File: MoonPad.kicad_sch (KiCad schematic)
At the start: 56 parts, among them IC1 W25Q16JVUXIQ, J1 OLED, J3 USB-C 2.0 Receptacle, SW1 Reset, U3 RP2040, U4 Hall_Sensor, U5 Hall_Sensor, U6 AP2112K-3.3, Y1 JGHC S3212000181080

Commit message: Added fuse
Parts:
- added D7: PRTR5V0U2X, Package_TO_SOT_SMD:SOT-143, symbol Power_Protection:PRTR5V0U2X
- added F1: Polyfuse, Fuse:Fuse_1206_3216Metric, symbol Device:Polyfuse
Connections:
- net GND: now also D7.1 (GND)
- net USB_D+: now also D7.2 (I/O1)
- net USB_D-: now also D7.3 (I/O2)
- net VBUS: now also D7.4 (VCC), F1.2; no longer J3.A4 (VBUS), J3.A9 (VBUS), J3.B4 (VBUS), J3.B9 (VBUS)
- new net Fuse: F1.1, J3.A4 (VBUS), J3.A9 (VBUS), J3.B4 (VBUS), J3.B9 (VBUS)
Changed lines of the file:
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@@
   (junction (at 207.01 81.28) (diameter 0) (color 0 0 0 0)
   )
-  (junction (at 57.15 35.56) (diameter 0) (color 0 0 0 0)
+  (junction (at 62.23 35.56) (diameter 0) (color 0 0 0 0)
   )
   (junction (at 355.6 160.02) (diameter 0) (color 0 0 0 0)
@@
     (stroke (width 0) (type default))
   )
-  (wire (pts (xy 57.15 34.29) (xy 57.15 35.56))
+  (wire (pts (xy 62.23 34.29) (xy 62.23 35.56))
     (stroke (width 0) (type default))
   )
@@
     (stroke (width 0) (type default))
   )
+  (wire (pts (xy 83.82 50.8) (xy 83.82 71.12))
+    (stroke (width 0) (type default))
+  )
   (wire (pts (xy 168.91 60.96) (xy 177.8 60.96))
     (stroke (width 0) (type default))
@@
     (stroke (width 0) (type default))
   )
+  (wire (pts (xy 59.69 35.56) (xy 62.23 35.56))
+    (stroke (width 0) (type default))
+  )
   (wire (pts (xy 204.47 81.28) (xy 207.01 81.28))
     (stroke (width 0) (type default))
@@
     (stroke (width 0) (type default))
   )
-  (wire (pts (xy 57.15 35.56) (xy 67.31 35.56))
+  (wire (pts (xy 62.23 35.56) (xy 67.31 35.56))
     (stroke (width 0) (type default))
   )
@@
     (stroke (width 0) (type default))
   )
+  (wire (pts (xy 52.07 35.56) (xy 49.53 35.56))
+    (stroke (width 0) (type default))
+  )
   (wire (pts (xy 67.31 44.45) (xy 67.31 45.72))
     (stroke (width 0) (type default))
   )
-  (wire (pts (xy 49.53 50.8) (xy 58.42 50.8))
+  (wire (pts (xy 49.53 50.8) (xy 83.82 50.8))
     (stroke (width 0) (type default))
   )
@@
     (stroke (width 0) (type default))
   )
+  (wire (pts (xy 58.42 55.88) (xy 58.42 71.12))
+    (stroke (width 0) (type default))
+  )
   (wire (pts (xy 269.24 62.23) (xy 269.24 60.96))
     (stroke (width 0) (type default))
@@
     (stroke (width 0) (type default))
   )
-  (wire (pts (xy 49.53 35.56) (xy 57.15 35.56))
-    (stroke (width 0) (type default))
-  )
   (wire (pts (xy 229.87 101.6) (xy 236.22 101.6))
     (stroke (width 0) (type default))
@@
     (effects (font (size 1.27 1.27)) (justify right bottom))
   )
+  (label "Fuse" (at 49.53 35.56 0) (fields_autoplaced)
+    (effects (font (size 1.27 1.27)) (justify left bottom))
+  )
   (label "USB_D+" (at 262.89 96.52 180) (fields_autoplaced)
     (effects (font (size 1.27 1.27)) (justify right bottom))
@@
     )
   )
-  (symbol (lib_id "power:VBUS") (at 57.15 34.29 0) (unit 1)
+  (symbol (lib_id "power:VBUS") (at 62.23 34.29 0) (unit 1)
     (in_bom yes) (on_board yes) (dnp no)
-    (property "Reference" "#PWR03" (at 57.15 38.1 0)
+    (property "Reference" "#PWR03" (at 62.23 38.1 0)
       (effects (font (size 1.27 1.27)) hide)
     )
-    (property "Value" "VBUS" (at 57.15 30.48 0)
+    (property "Value" "VBUS" (at 62.23 30.48 0)
       (effects (font (size 1.27 1.27)))
     )
-    (property "Footprint" "" (at 57.15 34.29 0)
+    (property "Footprint" "" (at 62.23 34.29 0)
       (effects (font (size 1.27 1.27)) hide)
     )
-    (property "Datasheet" "" (at 57.15 34.29 0)
+    (property "Datasheet" "" (at 62.23 34.29 0)
       (effects (font (size 1.27 1.27)) hide)
     )
@@
     )
   )
+  (symbol (lib_id "power:GND") (at 71.12 83.82 0) (unit 1)
+    (in_bom yes) (on_board yes) (dnp no) (fields_autoplaced)
+    (property "Reference" "#PWR047" (at 71.12 90.17 0)
+      (effects (font (size 1.27 1.27)) hide)
+    )
+    (property "Value" "GND" (at 71.12 88.9 0)
+      (effects (font (size 1.27 1.27)))
+    )
+    (property "Footprint" "" (at 71.12 83.82 0)
+      (effects (font (size 1.27 1.27)) hide)
+    )
+    (property "Datasheet" "" (at 71.12 83.82 0)
+      (effects (font (size 1.27 1.27)) hide)
+    )
+    (pin "1")
+    (instances
+      (project "MoonPad"
+        (path "/66a337f3-0e1a-4778-bb9f-853ccc5d3181"
+          (reference "#PWR047") (unit 1)
+        )
+      )
+    )
+  )
   (symbol (lib_id "power:GND") (at 69.85 124.46 0) (unit 1)
     (in_bom yes) (on_board yes) (dnp no)
@@
     )
   )
+  (symbol (lib_id "Device:Polyfuse") (at 55.88 35.56 90) (unit 1)
+    (in_bom yes) (on_board yes) (dnp no) (fields_autoplaced)
+    (property "Reference" "F1" (at 55.88 30.48 90)
+      (effects (font (size 1.27 1.27)))
+    )
+    (property "Value" "Polyfuse" (at 55.88 33.02 90)
+      (effects (font (size 1.27 1.27)))
+    )
+    (property "Footprint" "Fuse:Fuse_1206_3216Metric" (at 60.96 34.29 0)
+      (effects (font (size 1.27 1.27)) (justify left) hide)
+    )
+    (property "Datasheet" "https://datasheet.lcsc.com/lcsc/2103221807_BNstar-SMD1206-110C-24V_C2760273.pdf" (at 55.88 35.56 0)
+      (effects (font (size 1.27 1.27)) hide)
+    )
+    (property "LCSC Part" "https://www.lcsc.com/product-detail/Resettable-Fuses_BNstar-SMD1206-110C-24V_C2760273.html" (at 55.88 35.56 90)
+      (effects (font (size 1.27 1.27)) hide)
+    )
+    (pin "1")
+    (pin "2")
+    (instances
+      (project "MoonPad"
+        (path "/66a337f3-0e1a-4778-bb9f-853ccc5d3181"
+          (reference "F1") (unit 1)
+        )
+      )
+    )
+  )
   (symbol (lib_id "power:GND") (at 170.18 234.95 0) (unit 1)
     (in_bom yes) (on_board yes) (dnp no) (fields_autoplaced)
@@
     )
   )
+  (symbol (lib_id "Power_Protection:PRTR5V0U2X") (at 71.12 71.12 0) (unit 1)
+    (in_bom yes) (on_board yes) (dnp no) (fields_autoplaced)
+    (property "Reference" "D7" (at 86.36 69.1897 0)
+      (effects (font (size 1.27 1.27)))
+    )
+    (property "Value" "PRTR5V0U2X" (at 86.36 71.7297 0)
+      (effects (font (size 1.27 1.27)))
+    )
+    (property "Footprint" "Package_TO_SOT_SMD:SOT-143" (at 72.644 71.12 0)
+      (effects (font (size 1.27 1.27)) hide)
+    )
+    (property "Datasheet" "https://assets.nexperia.com/documents/data-sheet/PRTR5V0U2X.pdf" (at 72.644 71.12 0)
+      (effects (font (size 1.27 1.27)) hide)
+    )
+    (pin "1")
+    (pin "2")
+    (pin "3")
+    (pin "4")
+    (instances
+      (project "MoonPad"
+        (path "/66a337f3-0e1a-4778-bb9f-853ccc5d3181"
+          (reference "D7") (unit 1)
+        )
+      )
+    )
+  )
   (symbol (lib_id "Device:R") (at 59.69 116.84 270) (unit 1)
     (in_bom yes) (on_board yes) (dnp no)
@@
         )
       )
+    )
+  )
+  (symbol (lib_id "power:VBUS") (at 71.12 58.42 0) (unit 1)
+    (in_bom yes) (on_board yes) (dnp no)
+    (property "Reference" "#PWR048" (at 71.12 62.23 0)
+      (effects (font (size 1.27 1.27)) hide)
+    )
+    (property "Value" "VBUS" (at 71.12 54.61 0)
+      (effects (font (size 1.27 1.27)))
+    )
+    (property "Footprint" "" (at 71.12 58.42 0)
+      (effects (font (size 1.27 1.27)) hide)
+    )
+    (property "Datasheet" "" (at 71.12 58.42 0)
+      (effects (font (size 1.27 1.27)) hide)
+    )
+    (pin "1")
+    (instances
+      (project "MoonPad"
+        (path "/66a337f3-0e1a-4778-bb9f-853ccc5d3181"
+          (reference "#PWR048") (unit 1)
+        )
+      )

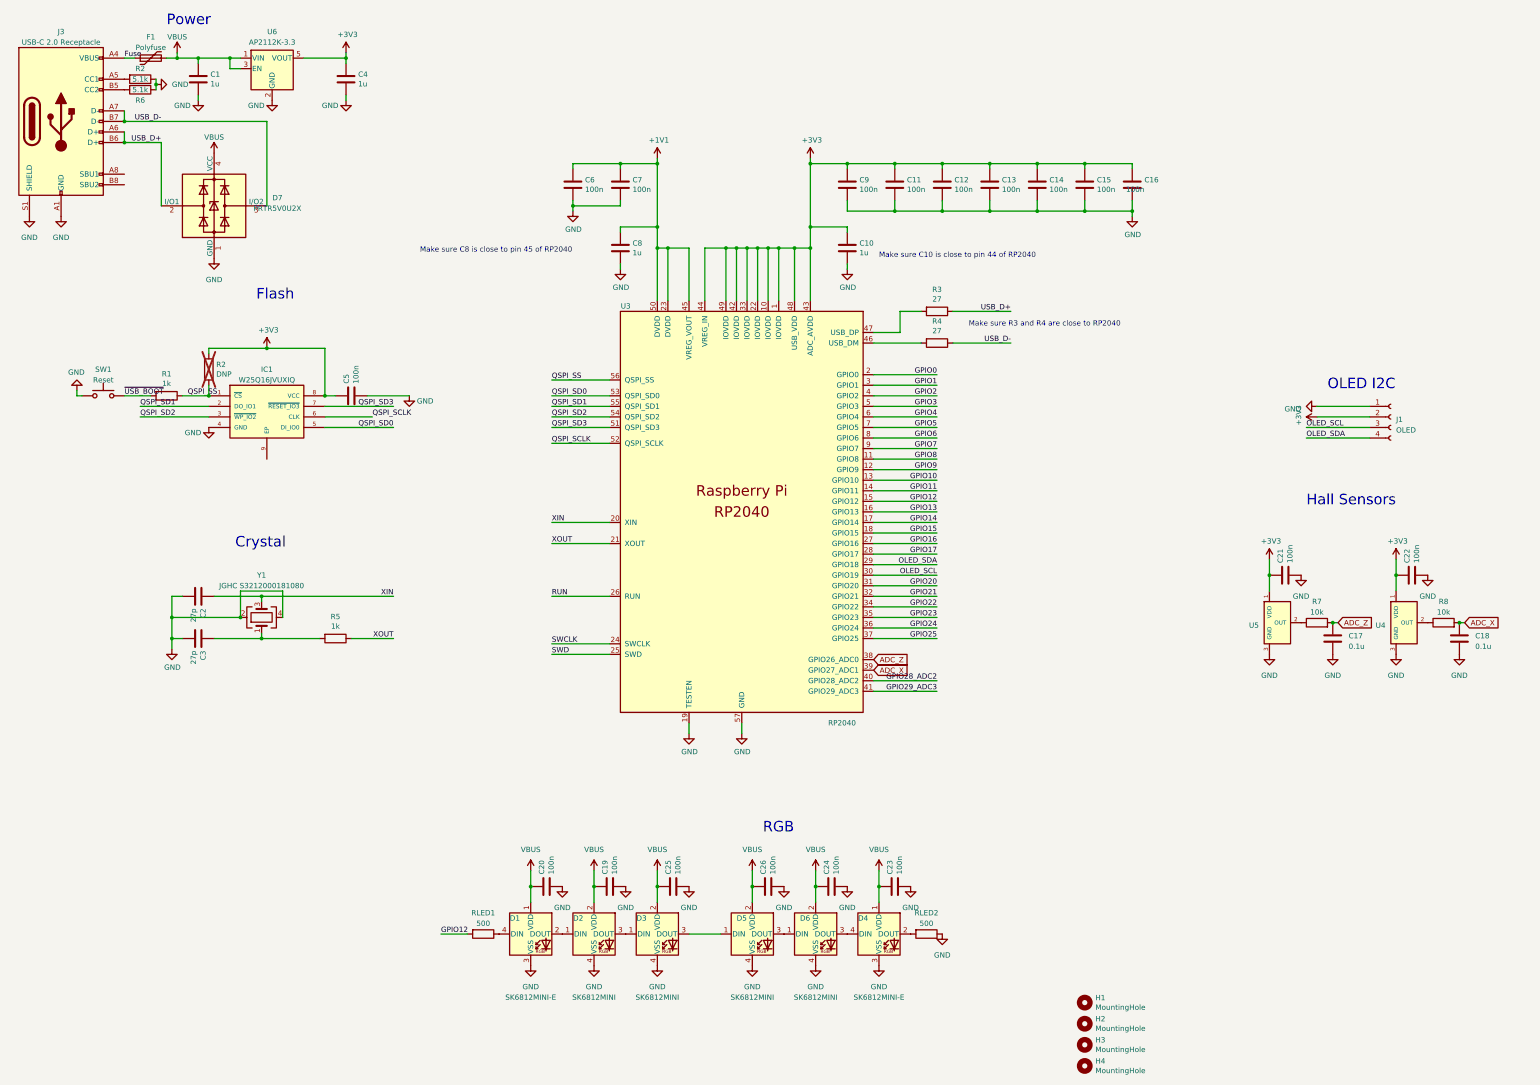
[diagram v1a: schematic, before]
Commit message: Added part numbers, some schema adjustments
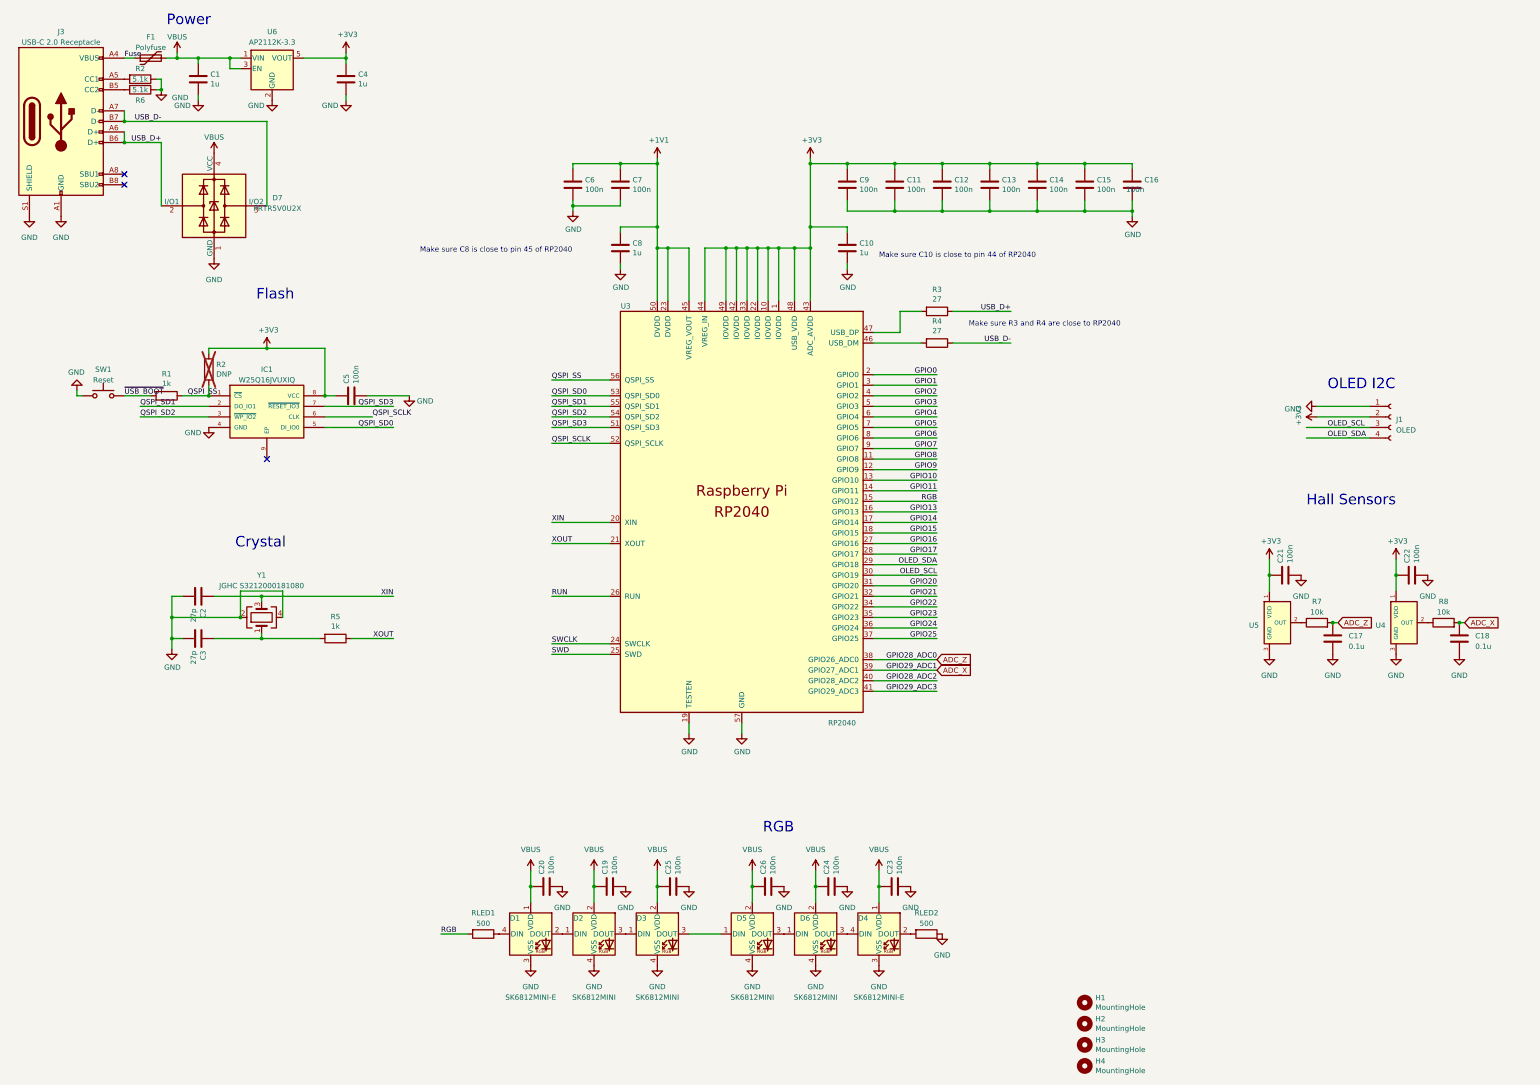
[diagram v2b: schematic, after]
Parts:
- C1, C4: LCSC Part (none) -> C28323
- D1, D4: footprint kicad-keyboard-parts:MX_SK6812MINI-E -> kicad-keyboard-parts:MX_SK6812MINI-E_REV
- R1, R5: LCSC Part (none) -> C25543
- R2, R6: LCSC Part (none) -> C25905
- R3, R4: LCSC Part (none) -> C25100
- R7, R8: LCSC Part (none) -> C25744
- RLED1, RLED2: footprint Resistor_SMD:R_0402_1005Metric -> Resistor_SMD:R_0805_2012Metric; LCSC Part (none) -> C2828857
- SW1: LCSC Part (none) -> C115351
- U3: footprint MoonPad:RP2040-QFN-56 -> Moonpad:RP2040-QFN-56
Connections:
- net GPIO12 renamed RGB
- no-connect marks 0 -> 3

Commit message: All part numbers added
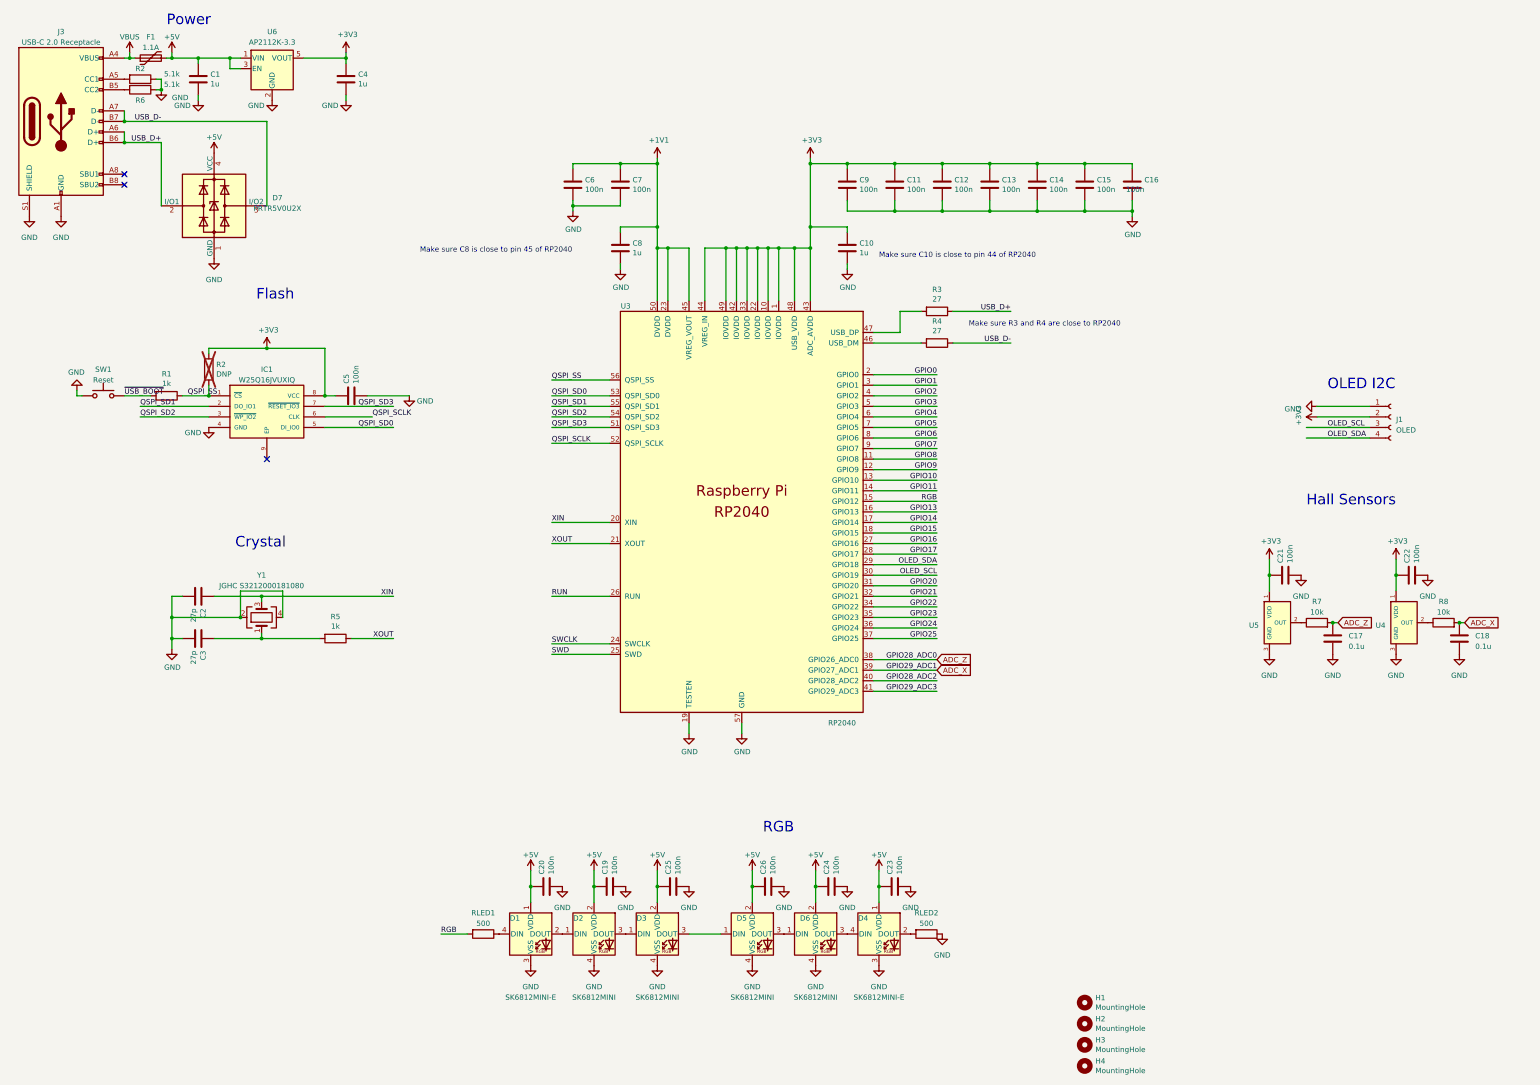
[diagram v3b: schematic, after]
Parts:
- C1, C4: LCSC (none) -> C28323
- C10, C8: LCSC (none) -> C52923
- C11, C12, C13, C14, C15, C16, C19, C20, C21, C22, C23, C24, C25, C26, C5, C6, C7, C9: LCSC (none) -> C1525
- C17, C18: footprint Capacitor_SMD:C_0402_1005Metric -> Capacitor_SMD:C_0201_0603Metric; LCSC (none) -> C5139511
- C2, C3: LCSC (none) -> C86287
- D1, D4: LCSC (none) -> C5149201
- D2, D3, D5, D6: LCSC (none) -> C5183448
- D7: LCSC (none) -> C2827688
- F1: value Polyfuse -> 1.1A; LCSC (none) -> C2760273
- IC1: LCSC (none) -> C2843335
- J3: LCSC (none) -> C165948
- R1, R5: LCSC (none) -> C25543
- R2: LCSC (none) -> C25905
- R3, R4: LCSC (none) -> C25100
- R6: LCSC (none) -> C25905; LCSC Part C25905 -> (none)
- R7, R8: footprint Resistor_SMD:R_0402_1005Metric -> Resistor_SMD:R_0201_0603Metric; LCSC (none) -> C25744
- RLED1, RLED2: LCSC (none) -> C2828857
- SW1: LCSC (none) -> C115351
- U3: LCSC (none) -> C2040
- U4, U5: value Hall_Sensor -> SLSS49E-3; LCSC (none) -> C2904393
- U6: LCSC (none) -> C51118; LCSC Part C51118 -> (none)
- Y1: LCSC (none) -> C390764
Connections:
- net Fuse is gone; now on net VBUS: F1.1, J3.A4 (VBUS), J3.A9 (VBUS), J3.B4 (VBUS), J3.B9 (VBUS)
- net VBUS: no longer C1.1, C19.1, C20.1, C23.1, C24.1, C25.1, C26.1, D1.1 (VDD), D2.2 (VDD), D3.2 (VDD), D4.1 (VDD), D5.2 (VDD), D6.2 (VDD), D7.4 (VCC), F1.2, U6.1 (VIN), U6.3 (EN)
- new net +5V: C1.1, C19.1, C20.1, C23.1, C24.1, C25.1, C26.1, D1.1 (VDD), D2.2 (VDD), D3.2 (VDD), D4.1 (VDD), D5.2 (VDD), D6.2 (VDD), D7.4 (VCC), F1.2, U6.1 (VIN), U6.3 (EN)

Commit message: Less extended parts
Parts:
- added C27: 100n, Capacitor_SMD:C_0402_1005Metric, symbol Device:C
- C17, C18: value 0.1u -> 100n; footprint Capacitor_SMD:C_0201_0603Metric -> Capacitor_SMD:C_0402_1005Metric
- R7, R8: footprint Resistor_SMD:R_0201_0603Metric -> Resistor_SMD:R_0402_1005Metric; LCSC Part C25744 -> (none)
- RLED1, RLED2: value 500 -> 470; footprint Resistor_SMD:R_0805_2012Metric -> Resistor_SMD:R_0402_1005Metric
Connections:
- net +3V3: now also C27.1
- net GND: now also C27.2
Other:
- moved on the sheet: C17, C18, C19, C2, C20, C21, C22, C23, C24, C25, C26, C3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

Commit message: Fixed libraries
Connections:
- no-connect marks 3 -> 31
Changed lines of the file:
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@@
   (junction (at 234.95 72.39) (diameter 0) (color 0 0 0 0)
   )
+  (no_connect (at 245.11 144.78))
+  (no_connect (at 152.4 165.1))
+  (no_connect (at 245.11 124.46))
+  (no_connect (at 245.11 114.3))
   (no_connect (at 93.98 134.62))
+  (no_connect (at 245.11 119.38))
   (no_connect (at 49.53 63.5))
+  (no_connect (at 245.11 121.92))
+  (no_connect (at 245.11 149.86))
   (no_connect (at 49.53 66.04))
+  (no_connect (at 245.11 111.76))
+  (no_connect (at 245.11 137.16))
+  (no_connect (at 152.4 176.53))
+  (no_connect (at 245.11 129.54))
+  (no_connect (at 245.11 147.32))
+  (no_connect (at 245.11 165.1))
+  (no_connect (at 245.11 167.64))
+  (no_connect (at 245.11 134.62))
+  (no_connect (at 245.11 139.7))
+  (no_connect (at 245.11 132.08))
+  (no_connect (at 245.11 172.72))
+  (no_connect (at 245.11 127))
+  (no_connect (at 245.11 116.84))
+  (no_connect (at 245.11 162.56))
+  (no_connect (at 245.11 187.96))
+  (no_connect (at 245.11 154.94))
+  (no_connect (at 245.11 152.4))
+  (no_connect (at 245.11 185.42))
+  (no_connect (at 245.11 175.26))
+  (no_connect (at 245.11 170.18))
+  (no_connect (at 152.4 179.07))
   (wire (pts (xy 229.87 144.78) (xy 245.11 144.78))
     (stroke (width 0) (type default))
@@
     (effects (font (size 1.27 1.27)) (justify left bottom))
   )
-  (label "GPIO27_ADC1" (at 245.11 182.88 180) (fields_autoplaced)
-    (effects (font (size 1.27 1.27)) (justify right bottom))
-  )
   (label "RUN" (at 152.4 165.1 0) (fields_autoplaced)
     (effects (font (size 1.27 1.27)) (justify left bottom))
@@
     (effects (font (size 1.27 1.27)) (justify right bottom))
   )
-  (label "GPIO26_ADC0" (at 245.11 180.34 180) (fields_autoplaced)
-    (effects (font (size 1.27 1.27)) (justify right bottom))
-  )
